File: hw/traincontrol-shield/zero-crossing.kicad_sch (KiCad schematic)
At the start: 3 parts, among them U2 H11AA1

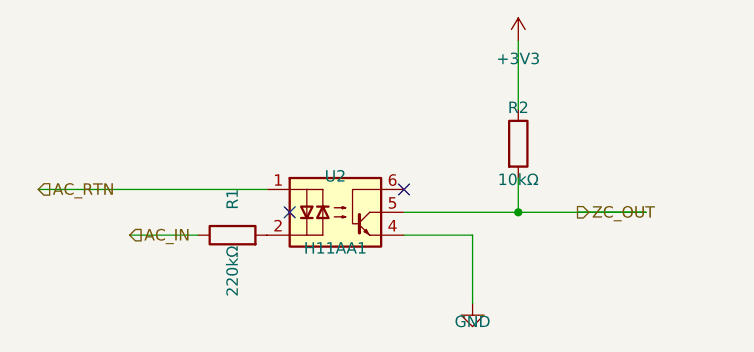
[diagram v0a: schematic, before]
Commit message: Fix hierarchical label placement and orientation in sub-sheets
Root cause: hlabel() placed the label at lx (stub tip) instead of x
(circuit connection point), mirroring the Issue-2 glabel bug fixed in
commit 2270223.

Fix applied to hlabel():
  (at {lx} ...) → (at {x} ...)  — label now sits at the circuit endpoint

Angle convention (matches label body direction):
  angle=180 → body extends LEFT  — left-side input/bidirectional labels
  angle=0   → body extends RIGHT — right-side output/bidirectional labels

Sheets affected: zero-crossing, xor-interlock, opto-triac-drive,
rail-voltage-sense; triacs-snubbers and mcu already had correct angles.

Co-Authored-By: Claude Sonnet 4.6 <noreply@anthropic.com>
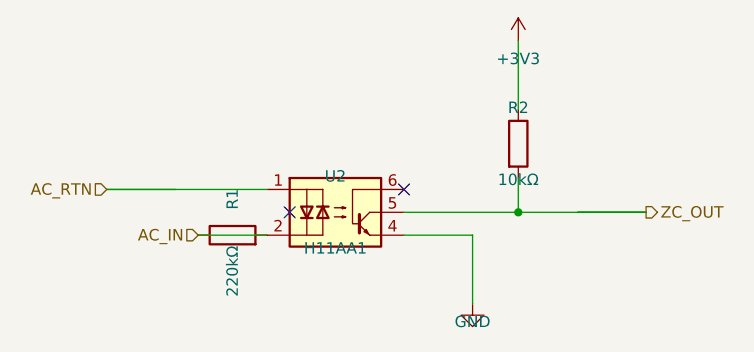
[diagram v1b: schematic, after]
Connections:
- net AC_IN: now also R1.2, U2.2
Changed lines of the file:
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@@
 	)
 	(wire
-		(pts (xy 73.66 92.71) (xy 81.28 92.71))
+		(pts (xy 81.28 92.71) (xy 88.9 92.71))
 		(stroke (width 0) (type solid))
 	)
 	(hierarchical_label "AC_IN"
 		(shape input)
-		(at 73.66 92.71 0)
+		(at 81.28 92.71 180)
 		(fields_autoplaced yes)
-		(effects (font (size 1.27 1.27)) (justify left bottom))
+		(effects (font (size 1.27 1.27)) (justify right bottom))
 		(property "Intersheetrefs" "${INTERSHEET_REFS}"
-			(at 73.66 92.71 0)
+			(at 81.28 92.71 0)
 			(effects (font (size 1.27 1.27)) (hide yes))
 		)
 	)
 	(wire
-		(pts (xy 63.50000000000001 87.63) (xy 71.12 87.63))
+		(pts (xy 71.12 87.63) (xy 78.74000000000001 87.63))
 		(stroke (width 0) (type solid))
 	)
 	(hierarchical_label "AC_RTN"
 		(shape input)
-		(at 63.50000000000001 87.63 0)
+		(at 71.12 87.63 180)
 		(fields_autoplaced yes)
-		(effects (font (size 1.27 1.27)) (justify left bottom))
+		(effects (font (size 1.27 1.27)) (justify right bottom))
 		(property "Intersheetrefs" "${INTERSHEET_REFS}"
-			(at 63.50000000000001 87.63 0)
+			(at 71.12 87.63 0)
 			(effects (font (size 1.27 1.27)) (hide yes))
 		)
@@
 	(hierarchical_label "ZC_OUT"
 		(shape output)
-		(at 123.41999999999999 90.17 0)
+		(at 131.04 90.17 0)
 		(fields_autoplaced yes)
 		(effects (font (size 1.27 1.27)) (justify left bottom))
 		(property "Intersheetrefs" "${INTERSHEET_REFS}"
-			(at 123.41999999999999 90.17 0)
+			(at 131.04 90.17 0)
 			(effects (font (size 1.27 1.27)) (hide yes))
 		)

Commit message: Fix hlabel stub short-circuits on zero-crossing and power-supply pages
The hlabel() stub wire ran from the circuit pin inward, crossing directly
over series components and creating short-circuits:
- zero-crossing AC_IN: stub spanned R1 (x 81.28→88.90); shift x to 73.66
- power-supply AC_IN:  stub crossed D1 body (x 40.64→48.26); shift x to 33.02
- power-supply AC_RTN: same; shift x to 33.02

Pattern: for angle=180 labels, x = component_inner_pin - STUB so the
stub terminates at the component outer pin rather than spanning across it.

All 8 sheets validate with kicad-cli.

Co-Authored-By: Claude Sonnet 4.6 <noreply@anthropic.com>
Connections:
- net AC_IN: no longer R1.2, U2.2
- new net: R1.2, U2.2
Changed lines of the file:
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@@
 	)
 	(wire
-		(pts (xy 81.28 92.71) (xy 88.9 92.71))
+		(pts (xy 73.66 92.71) (xy 81.28 92.71))
 		(stroke (width 0) (type solid))
 	)
 	(hierarchical_label "AC_IN"
 		(shape input)
-		(at 81.28 92.71 180)
+		(at 73.66 92.71 180)
 		(fields_autoplaced yes)
 		(effects (font (size 1.27 1.27)) (justify right bottom))
 		(property "Intersheetrefs" "${INTERSHEET_REFS}"
-			(at 81.28 92.71 0)
+			(at 73.66 92.71 0)
 			(effects (font (size 1.27 1.27)) (hide yes))
 		)

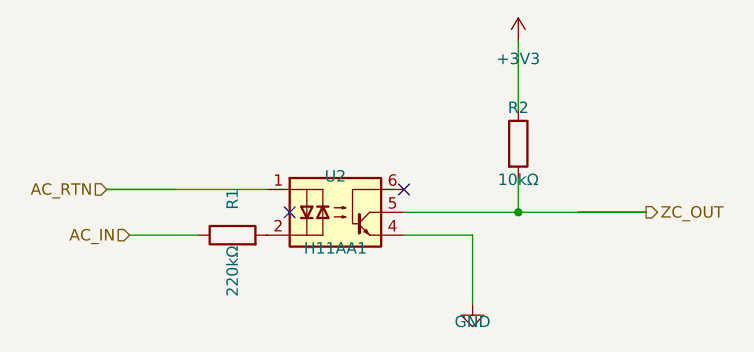
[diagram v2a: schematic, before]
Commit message: Fix hlabel stub direction: stubs now extend away from IC, not into it
Root cause: hlabel() used dx = +STUB for angle=180 and -STUB for angle=0,
which caused every stub wire to run INTO the IC body instead of outward.
This made wires appear to connect at the inner (wrong) end of all pins.

Fix: negate dx so stubs always extend outward from the pin tip:
  angle=180 (left-side input):  dx = -STUB → stub extends LEFT  ✓
  angle=0   (right-side output): dx = +STUB → stub extends RIGHT ✓

Also revert the x-position workarounds that compensated for the wrong
stub direction (zero-crossing AC_IN, opto-triac PHASE/GATE, power-supply
AC_IN/RTN): these are now back at the actual component pin positions.

All 8 sheets validate with kicad-cli.

Co-Authored-By: Claude Sonnet 4.6 <noreply@anthropic.com>
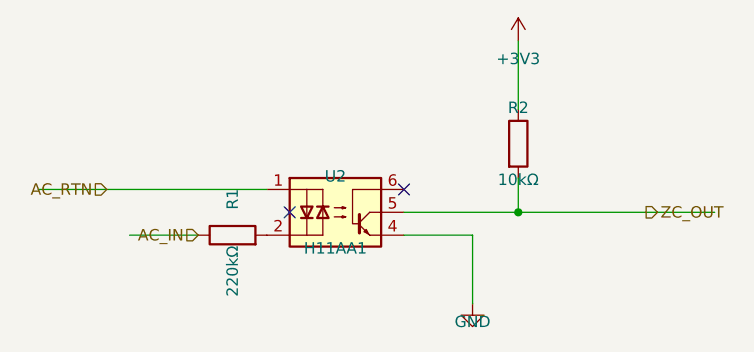
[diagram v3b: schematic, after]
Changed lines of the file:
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@@
 	(hierarchical_label "AC_IN"
 		(shape input)
-		(at 73.66 92.71 180)
+		(at 81.28 92.71 180)
 		(fields_autoplaced yes)
 		(effects (font (size 1.27 1.27)) (justify right bottom))
 		(property "Intersheetrefs" "${INTERSHEET_REFS}"
-			(at 73.66 92.71 0)
+			(at 81.28 92.71 0)
 			(effects (font (size 1.27 1.27)) (hide yes))
 		)
 	)
 	(wire
-		(pts (xy 71.12 87.63) (xy 78.74000000000001 87.63))
+		(pts (xy 63.50000000000001 87.63) (xy 71.12 87.63))
 		(stroke (width 0) (type solid))
 	)
@@
 	)
 	(wire
-		(pts (xy 123.41999999999999 90.17) (xy 131.04 90.17))
+		(pts (xy 131.04 90.17) (xy 138.66 90.17))
 		(stroke (width 0) (type solid))
 	)
